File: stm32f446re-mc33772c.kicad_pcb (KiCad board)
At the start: 4 copper layers, 105.7 x 62.5 mm, 120 parts, among them J1 Conn_01x02, J2 USB_B_Micro, J3 Conn_01x03, J4 Conn_01x03, J5 S7B-XH-A, J6 SM06B-GHS-TB, U1 STM32F446RETx, U2 MC33772CTP1AE, U3 LD1086D2M33TR, U4 AMS1117-3.3, U6 LMR51450SDRRR, U7 SN65HVD232, Y1 16MHz

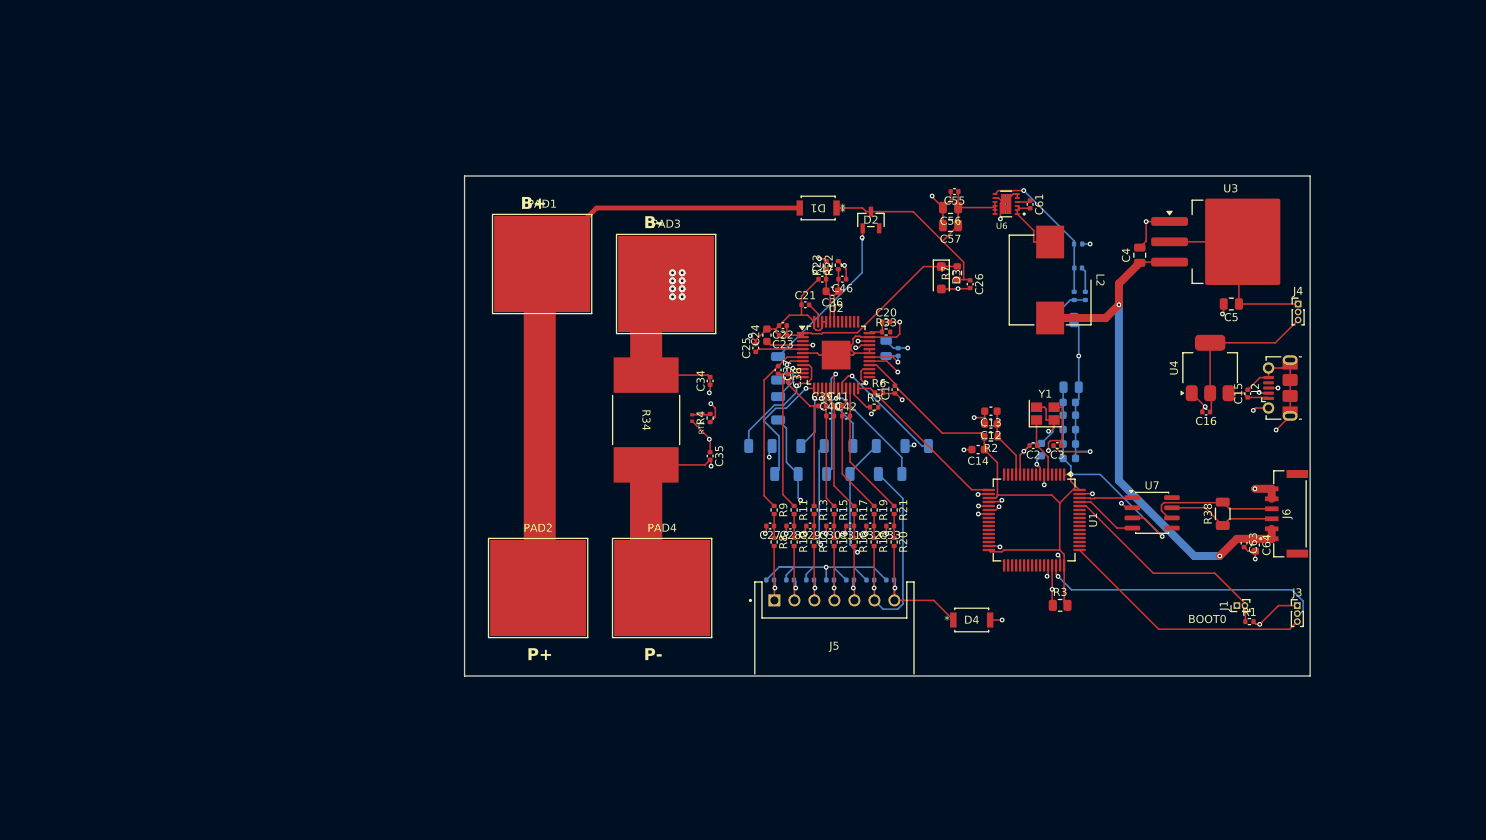
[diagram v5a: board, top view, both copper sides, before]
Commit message: GND, power_flag
1. F.Cu and B.Cu fill zone with GND
2. add power_flag
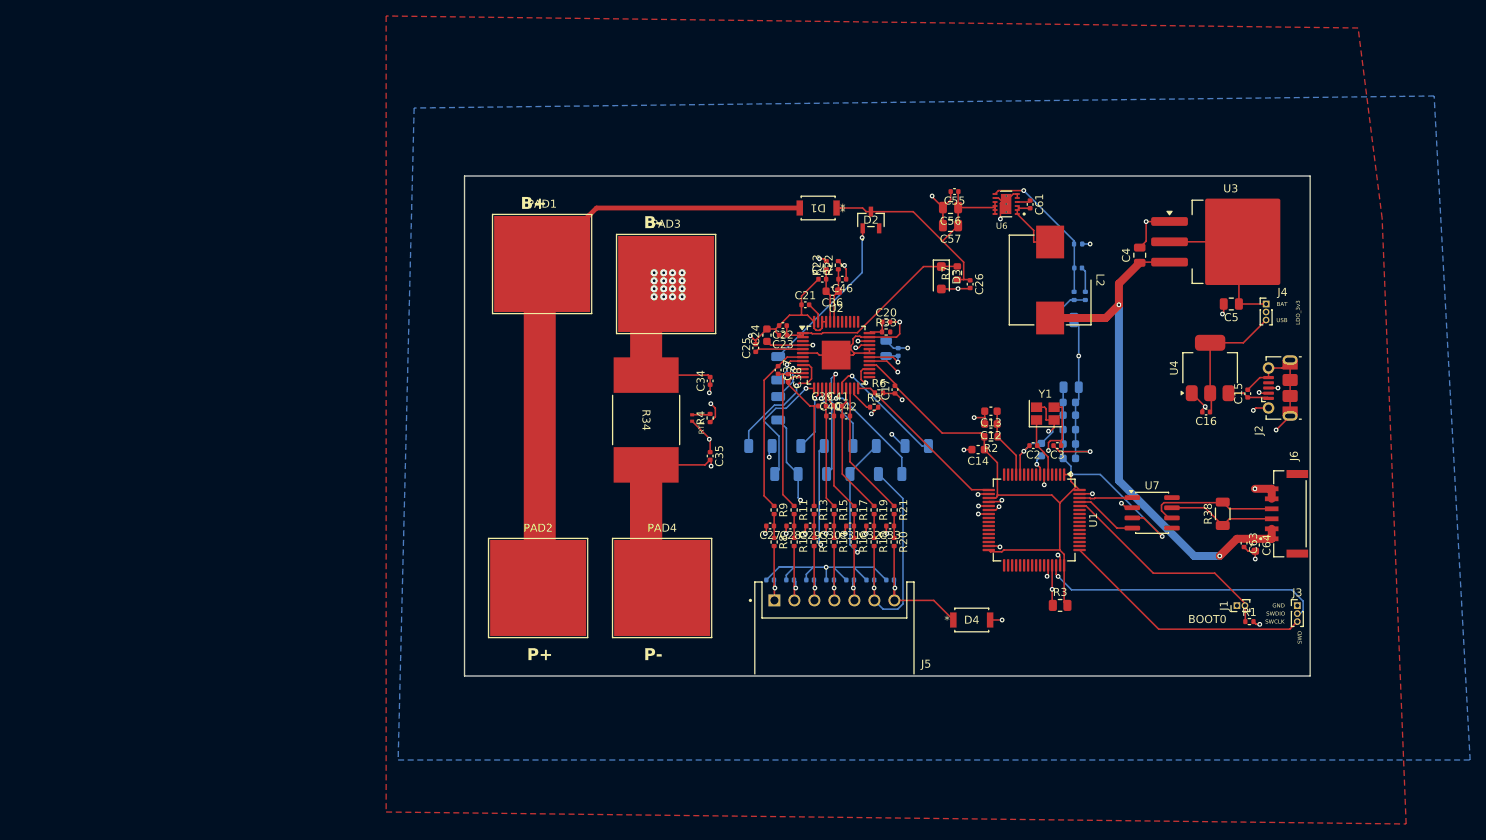
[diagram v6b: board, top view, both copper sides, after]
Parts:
- moved J4 4.00 mm to (215.0, 56.5)
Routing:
- net Rsense_P: track 195.1 -> 189.4 mm, vias 44 -> 52
- net USB_3.3V: track 21.0 -> 17.0 mm
- net BAT_3.3V: track 23.8 -> 19.8 mm
- net LDO_3.3V: track 144.7 -> 146.9 mm
- net BP-C1M: track 48.4 -> 49.5 mm
- added copper zone on B.Cu, net Rsense_P
- added copper zone on F.Cu, net Rsense_P
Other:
- board text added: "BAT"
- board text added: "GND"
- board text added: "LDO_3v3"
- board text added: "SWCLK"
- board text added: "SWD"
- board text added: "SWDIO"
- board text added: "USB"

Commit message: no error in DRC
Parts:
- J1: footprint Connector_PinHeader_1.00mm:PinHeader_1x02_P1.00mm_Vertical -> Connector_PinHeader_2.54mm:PinHeader_1x02_P2.54mm_Vertical
- J3, J4: footprint Connector_PinHeader_1.00mm:PinHeader_1x03_P1.00mm_Vertical -> Connector_PinHeader_2.54mm:PinHeader_1x03_P2.54mm_Vertical
- moved C5 6.40 mm to (205.0, 59.5)
- moved J4 5.83 mm to (210.0, 59.5), turned to 90 degrees
- moved J1 4.18 mm to (207.2, 93.5)
- moved R1 2.70 mm to (212.9, 93.5)
- moved J2 2.59 mm to (216.8, 69.6)
- moved C15 2.16 mm to (212.2, 69.8)
- moved C16 2.16 mm to (207.0, 72.1)
- moved U4 2.16 mm to (207.5, 66.6)
- moved J3 1.75 mm to (218.5, 92.5)
- moved C63 1.74 mm to (210.5, 86.5)
- moved R38 1.57 mm to (208.0, 82.7)
- moved R33 1.51 mm to (167.5, 58.5)
- moved J6 1.19 mm to (216.4, 82.8)
- moved C64 1.19 mm to (212.5, 86.7)
- moved C4 1.12 mm to (198.2, 50.9)
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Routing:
- net Rsense_P: track 189.4 -> 220.0 mm, vias 52 -> 55
- net Net-(R33-Pad2): track 2.45 -> 33.0 mm, vias 0 -> 2
- net BP-C6P: track 79.5 -> 57.1 mm, vias 2 -> 3
- net AFE_VCOM: track 34.7 -> 56.8 mm
- net Pack-: track 73.0 -> 55.9 mm, vias 2 -> 0
- net BP-C1M: track 49.5 -> 37.0 mm, vias 5 -> 2
- net LDO_3.3V: track 146.9 -> 134.4 mm
- net BAT_3.3V: track 19.8 -> 25.6 mm
- net D-: track 41.3 -> 38.2 mm
- net Net-(J1-Pin_2): track 28.0 -> 25.6 mm
- net SWDIO: track 35.5 -> 33.6 mm
- net Net-(U6-SW): track 8.98 -> 7.33 mm
- net D+: track 46.8 -> 48.1 mm
- net CANH: track 13.7 -> 12.5 mm
- net CANL: track 16.7 -> 15.5 mm
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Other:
- board size 105.7 x 62.5 mm -> 105.3 x 62.5 mm

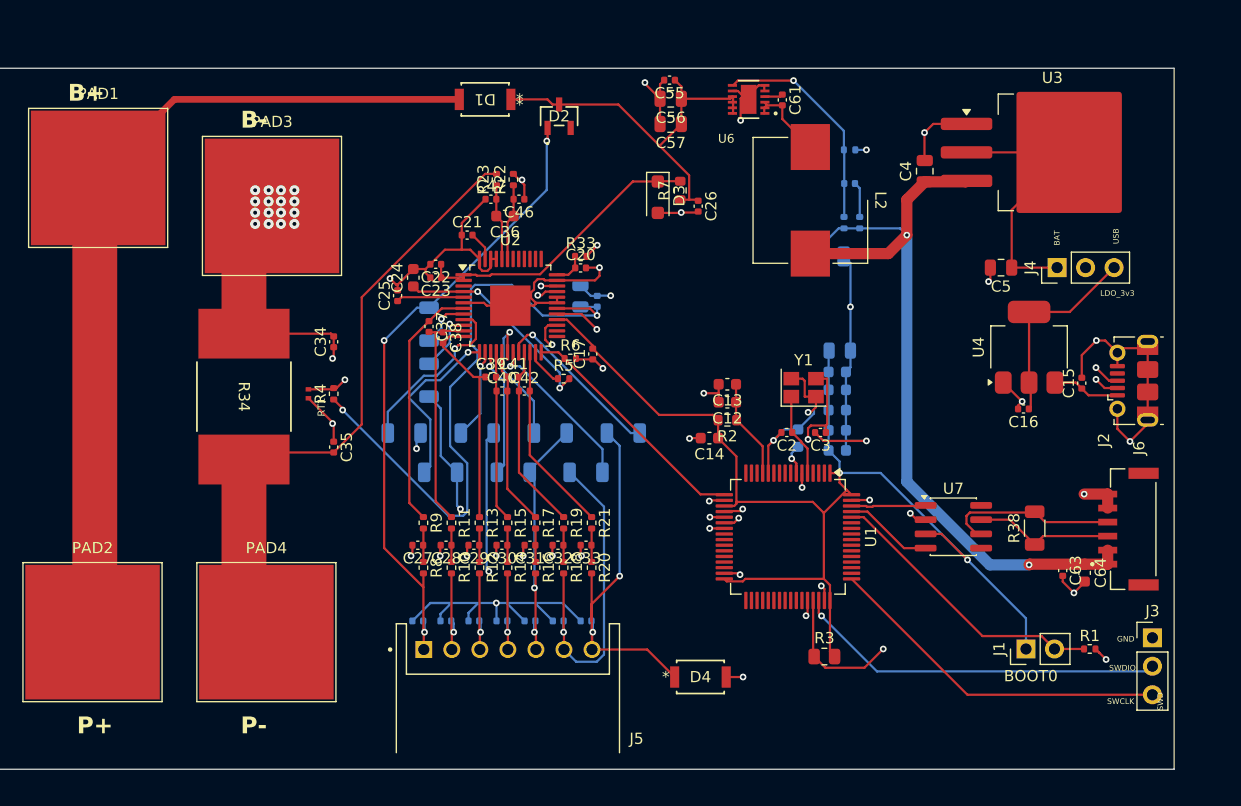
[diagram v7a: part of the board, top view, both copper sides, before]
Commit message: DRC: remove silkscreen warning
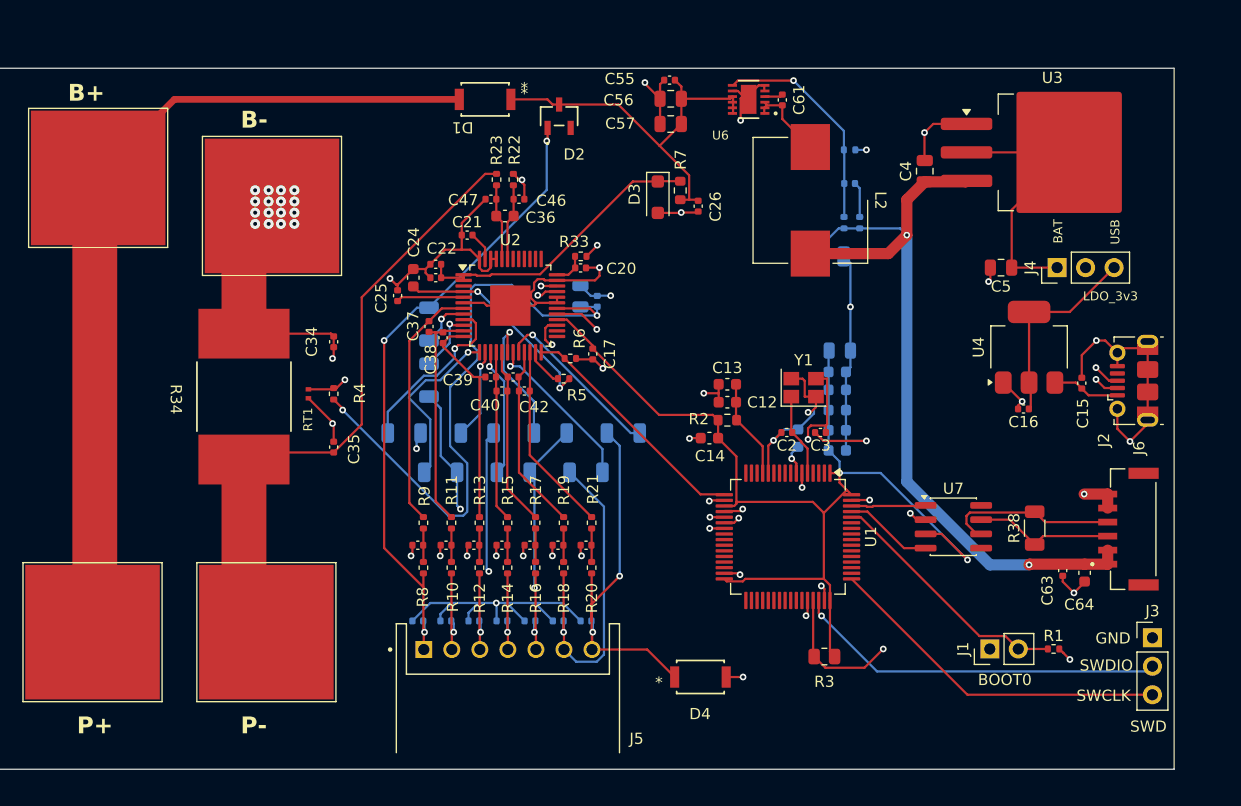
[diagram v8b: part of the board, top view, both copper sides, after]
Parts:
- moved J1 3.22 mm to (204.0, 93.5)
- moved R1 3.22 mm to (209.7, 93.5)
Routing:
- net Net-(J1-Pin_2): track 25.6 -> 22.4 mm
- net LDO_3.3V: track 134.4 -> 133.1 mm
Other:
- board text added: "*"
